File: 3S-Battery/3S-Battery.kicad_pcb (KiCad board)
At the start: 2 copper layers, 31 parts, among them J1 Conn_01x04, J2 Conn_01x02, Q3 BSS84, Q4 AO4892, U3 BQ76920PW

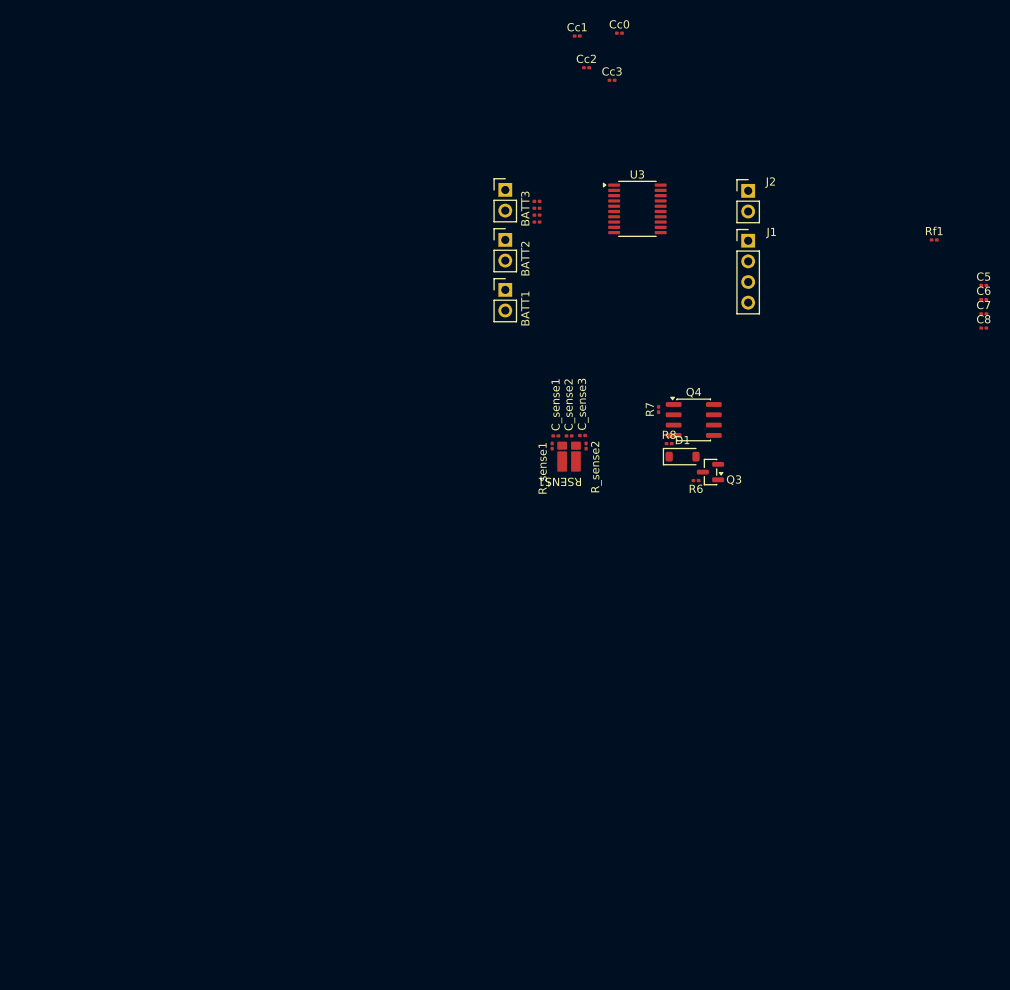
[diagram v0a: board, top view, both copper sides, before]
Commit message: Add new components and update existing ones in easyeda2kicad library
- Added BAT-SMD_BH-18650-B5BA016 module for battery SMD.
- Added HDR-TH_2P-P2.54-V-M-3 and HDR-TH_4P-P2.54-V-M-1 modules for through-hole headers.
- Introduced R0612, R2512, and R2728 modules for resistors.
- Updated R0805 module to reference the correct 3D model file.
- Added RES-SMD_4P-L3.2-W1.6_CSSK0612 and RES-SMD_L6.4-W3.2-R2512 modules for SMD resistors.
- Added SO-8_L4.9-W3.9-P1.27-LS5.9-BL module for SOIC package.
- Added SW-SMD_L3.9-W3.0-P4.45 module for SMD switch.
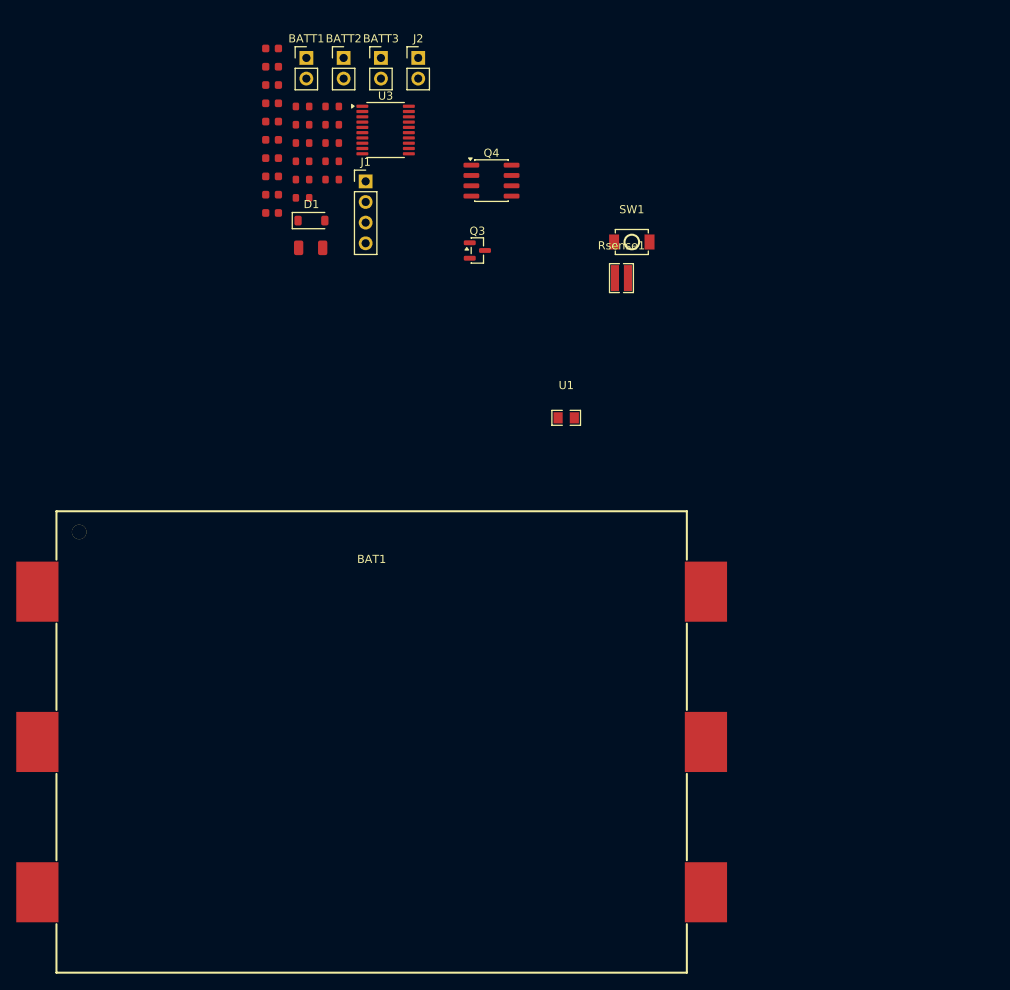
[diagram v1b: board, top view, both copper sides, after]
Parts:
- removed C7, Cc2, Cc3: 0.1u, Capacitor_SMD:C_0201_0603Metric
- removed C8: 4.7u, Capacitor_SMD:C_0201_0603Metric
- removed R6, R7, R8: 1M, Resistor_SMD:R_0201_0603Metric
- removed RSENS1: 15m, Resistor_SMD:CSSK0612FT5L00
- removed Rf1: 10, Resistor_SMD:R_0201_0603Metric
- added BAT1: BH-18650-B5BA016, easyeda2kicad:BAT-SMD_BH-18650-B5BA016, F.Cu at (85.5, 124.7)
- added C1: 1uF, PCM_JLCPCB:C_1206, F.Cu at (77.9, 63.9)
- added C2: 10uF, PCM_JLCPCB:C_0603, F.Cu at (73.2, 39.3)
- added C3: 1uF, PCM_JLCPCB:C_0603, F.Cu at (73.2, 41.6)
- added C4: 4.7uF, PCM_JLCPCB:C_0603, F.Cu at (73.2, 43.8)
- added R1: 10kΩ, PCM_JLCPCB:R_0603, F.Cu at (76.9, 46.5)
- added R2: 100Ω, PCM_JLCPCB:R_0603, F.Cu at (76.9, 48.7)
- added R3: 1MΩ, PCM_JLCPCB:R_0603, F.Cu at (76.9, 51.0)
- added R4: 1MΩ, PCM_JLCPCB:R_0603, F.Cu at (76.9, 53.2)
- added R5: 1MΩ, PCM_JLCPCB:R_0603, F.Cu at (76.9, 55.5)
- added Rsense1: LTR18EZPFSR015, easyeda2kicad:R0612, F.Cu at (116.2, 67.6)
- added SW1: TS-1088R-02026, easyeda2kicad:SW-SMD_L3.9-W3.0-P4.45, F.Cu at (117.5, 63.2)
- added U1: NTC10K/0805/F, easyeda2kicad:R0805, F.Cu at (109.4, 84.8)
- C5, C6: value 1u -> 1uF; footprint Capacitor_SMD:C_0201_0603Metric -> PCM_JLCPCB:C_0603
- C_sense1, C_sense2, C_sense3: value 0.1u -> 100nF; footprint Capacitor_SMD:C_0201_0603Metric -> PCM_JLCPCB:C_0603
- Cc0, Cc1: value 0.1u -> 1uF; footprint Capacitor_SMD:C_0201_0603Metric -> PCM_JLCPCB:C_0603
- R_sense1, R_sense2, Rc0, Rc1, Rc2, Rc3: value 100 -> 100Ω; footprint Resistor_SMD:R_0201_0603Metric -> PCM_JLCPCB:R_0603
- moved C5 90.4 mm to (73.2, 46.1)
- moved C6 90.3 mm to (73.2, 48.3)
- moved D1 54.1 mm to (78.0, 60.5)
- moved R_sense2 52.2 mm to (80.6, 46.5), turned to 0 degrees
- moved C_sense1 50.5 mm to (73.2, 50.6)
- moved C_sense2 50.1 mm to (73.2, 52.8)
- moved C_sense3 49.8 mm to (73.2, 55.1)
- moved J1 47.7 mm to (84.7, 55.7)
- moved Cc0 47.2 mm to (73.2, 57.3)
- moved J2 43.8 mm to (91.2, 40.5)
- moved Cc1 43.4 mm to (73.2, 59.6)
- moved R_sense1 43.3 mm to (76.9, 57.7), turned to 0 degrees
- moved Q3 39.6 mm to (98.5, 64.2), turned to 0 degrees
- moved Q4 38.6 mm to (100.2, 55.6)
- moved BATT1 37.6 mm to (77.4, 40.5)
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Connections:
- C5 pad 1: /GND -> Net-(U3-VC3)
- C5 pad 2: Net-(U3-BAT) -> Net-(U3-VC2)
- C6 pad 1: /GND -> Net-(U3-VC2)
- C6 pad 2: /PACK+ -> /VC1
- Cc1 pad 1: Net-(U3-VC1) -> /VC1
- R_sense1 pad 2: Net-(RSENS1-Pad2) -> /PROTECT-
- R_sense2 pad 2: Net-(RSENS1-Pad3) -> /GND
- Rc0 pad 1: /GND -> Net-(U3-VC0)
- Rc0 pad 2: Net-(U3-VC0) -> /GND
- Rc1 pad 1: Net-(BATT1-Pin_1) -> /VC1
- Rc1 pad 2: Net-(U3-VC1) -> Net-(BATT1-Pin_1)
- Rc2 pad 1: Net-(BATT2-Pin_1) -> Net-(U3-VC2)
- Rc2 pad 2: Net-(U3-VC2) -> Net-(BATT2-Pin_1)
- Rc3 pad 1: /PACK+ -> Net-(U3-VC3)
- Rc3 pad 2: Net-(U3-VC3) -> /PACK+
- U3 pad 16: Net-(U3-VC1) -> /VC1
- U3 pad 6: unconnected-(U3-TS1-Pad6) -> Net-(U3-TS1)
- U3 pad 8: Net-(U3-REGOUT) -> /VCC
